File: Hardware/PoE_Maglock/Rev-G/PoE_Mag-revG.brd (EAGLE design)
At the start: 72.8 x 47.9 mm, 85 parts, among them IC2 ATMEGA32U4-MU, J2 1X2-3.5MM, J3 1X2-3.5MM, J4 1X2-3.5MM, J5 1X2-3.5MM, J6 10103594-0001LF, Q1 35A/25V/8.5mΩ, Q3 35A/25V/8.5mΩ, Q5 35A/25V/8.5mΩ, Q6 35A/25V/8.5mΩ, SW1 SPST_TACT-KMR2, U4 W5500, X2 J1011FHY931147C, Y4 8MHz

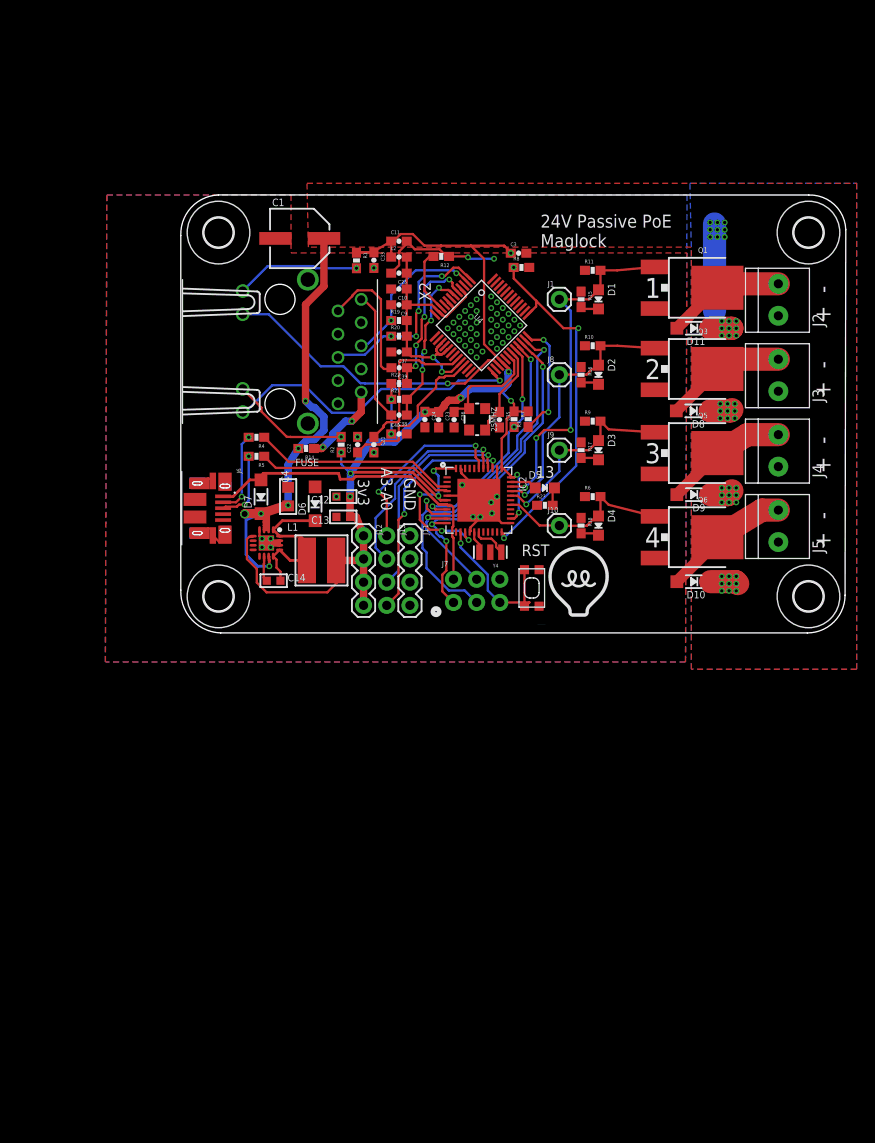
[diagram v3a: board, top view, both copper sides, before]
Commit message: HEEP-1046 added analog terminal blocks to schematic
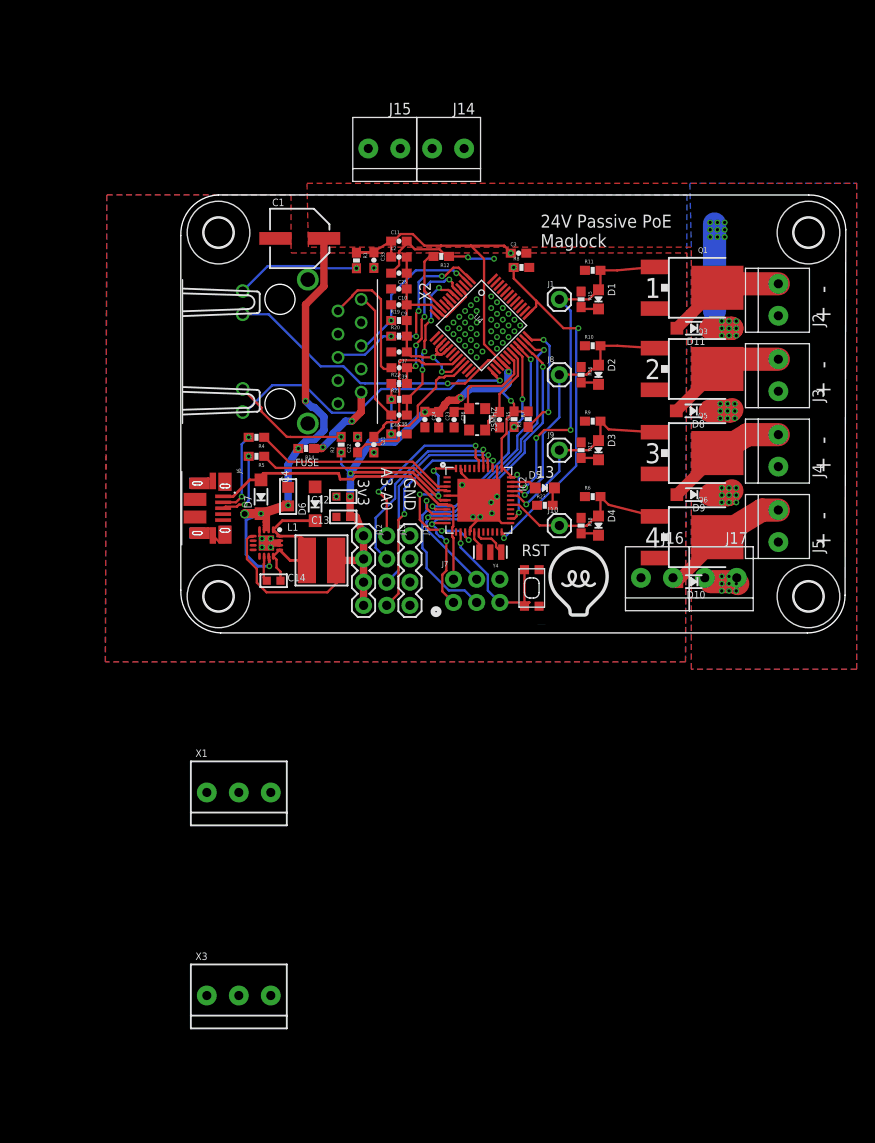
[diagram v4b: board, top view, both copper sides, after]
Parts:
- added J14, J15, J16, J17: 1X2-3.5MM, adafruit:1X2-3.5MM
- added X1, X3: (no value), microbuilder:TERMBLOCK_1X3-3.5MM
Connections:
- removed net 0: IC2.20
- removed net 1: IC2.21
- removed net 2: IC2.19
- removed net 3: IC2.18
- new net 0/RX: IC2.20, J17.2
- new net 1/TX: IC2.21, J17.1
- new net 2/SDA: IC2.19, J15.1
- new net 3/SCL: IC2.18, J15.2
- net +3V3: now also J14.1, J16.1, X1.3, X3.3
- net GND: now also J14.2, J16.2, X1.1, X3.1

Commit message: HEEP-1046 added DC jack to schematic and to brd. not yet positioned
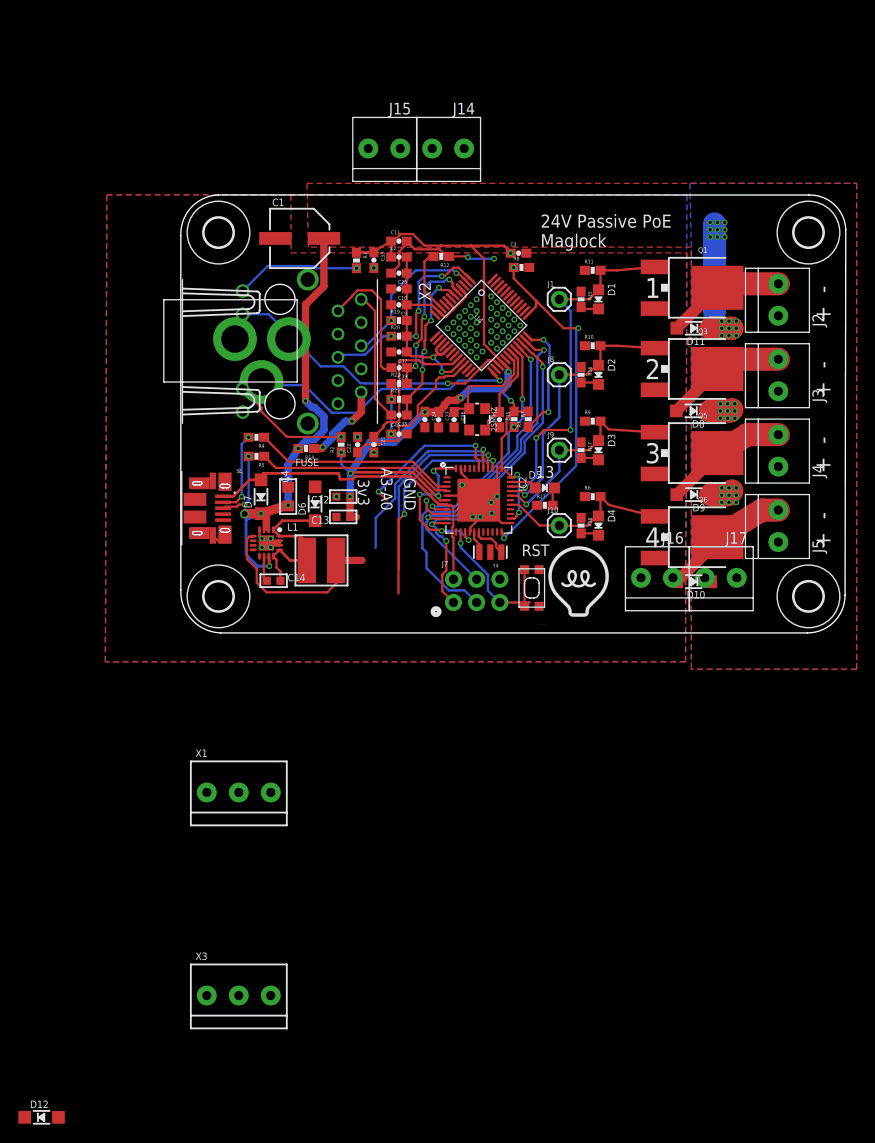
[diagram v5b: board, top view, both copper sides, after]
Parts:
- removed J11, J12: (no value), SparkFun-Connectors:1X04
- removed J13: (no value), SparkFun-Connectors:1X04_NO_SILK
- added D12: PMEG4030ER, microbuilder:SOD-123
- added U$4: 2.1MMJACKTHM, adafruit:PJ-102A
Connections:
- new net N$1: D12.A, U$4.TIP
- net +3V3: no longer J12.1, J12.2, J12.3, J12.4
- net A0: no longer J13.4
- net A1: no longer J13.3
- net A2: no longer J13.2
- net A3: no longer J13.1
- net GND: now also U$4.RING, U$4.RING_SW; no longer J11.1, J11.2, J11.3, J11.4
- net VBAT: now also D12.C
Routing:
- net +3V3: track 148.3 -> 137.4 mm
- net A3: track 20.5 -> 16.6 mm
- net VBAT: track 77.9 -> 74.8 mm, vias 51 -> 42
- net A1: track 24.3 -> 22.4 mm
- net A0: track 25.4 -> 23.6 mm
- net A2: track 22.9 -> 21.2 mm

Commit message: HEEP-1046 extended southside
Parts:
- added J11: 1X2-3.5MM, adafruit:1X2-3.5MM
- moved D12 66.1 mm to (2.54, 10.8), turned to 90 degrees
- moved U$15 57.9 mm to (46.7, 57.8)
- moved X3 49.8 mm to (33.4, 3.81)
- moved X1 24.7 mm to (21.6, 3.81)
- moved J6 8.25 mm to (6.25, 21.0)
- moved C1 7.94 mm to (17.5, 50.2)
- moved C3 7.62 mm to (41.4, 48.2)
- moved C33 7.62 mm to (25.6, 47.5)
- moved D11 7.62 mm to (60.6, 40.0)
- moved H1 7.62 mm to (73.1, 50.5)
- moved H3 7.62 mm to (8.57, 50.5)
- moved Q1 7.62 mm to (61.6, 44.5)
- moved X2 7.62 mm to (15.3, 37.5)
- moved 25MHZ 7.62 mm to (36.9, 30.0)
- moved C21 7.62 mm to (25.6, 27.3)
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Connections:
- removed net N$2: R14.1, X2.9
- new net POE+: D12.C, R14.1, X2.9
- net GND: now also J11.2
- net VBAT: now also J11.1; no longer D12.C
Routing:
- net VBAT: track 74.8 -> 56.5 mm, vias 42 -> 41
- net POE+: track 0.00 -> 9.23 mm, vias 0 -> 2
- net N$2: track 9.23 -> 0.00 mm, vias 2 -> 0
- net A1: track 22.4 -> 13.3 mm
- net A0: track 23.6 -> 14.6 mm, vias 2 -> 1
- net A2: track 21.2 -> 13.4 mm
- net +3V3: track 137.4 -> 139.3 mm
- net A3: track 16.6 -> 15.3 mm, vias 2 -> 1
- net N$13: track 9.10 -> 8.47 mm
- net VBUS: track 37.2 -> 36.6 mm
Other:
- board size 72.8 x 47.9 mm -> 72.8 x 53.3 mm

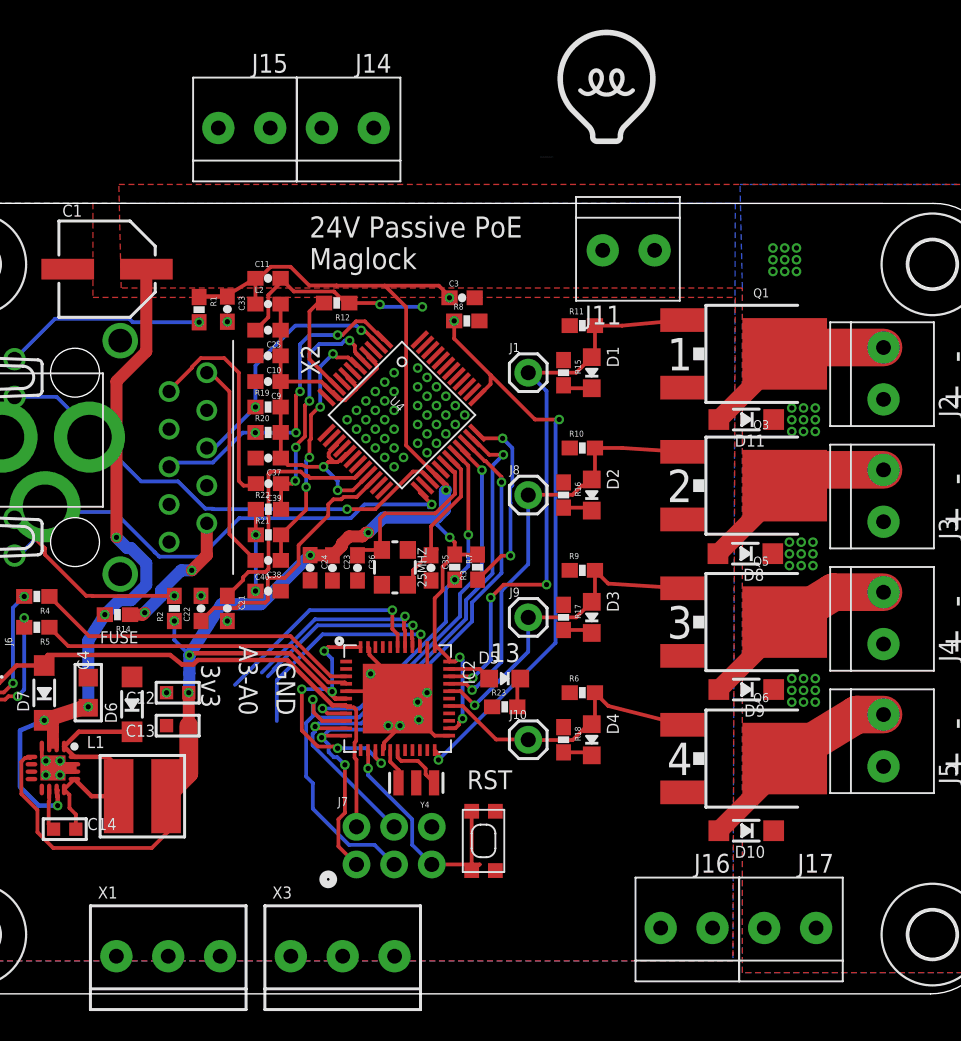
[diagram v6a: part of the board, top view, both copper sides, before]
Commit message: HEEP-1046 before rotating buck circuit 90 degrees
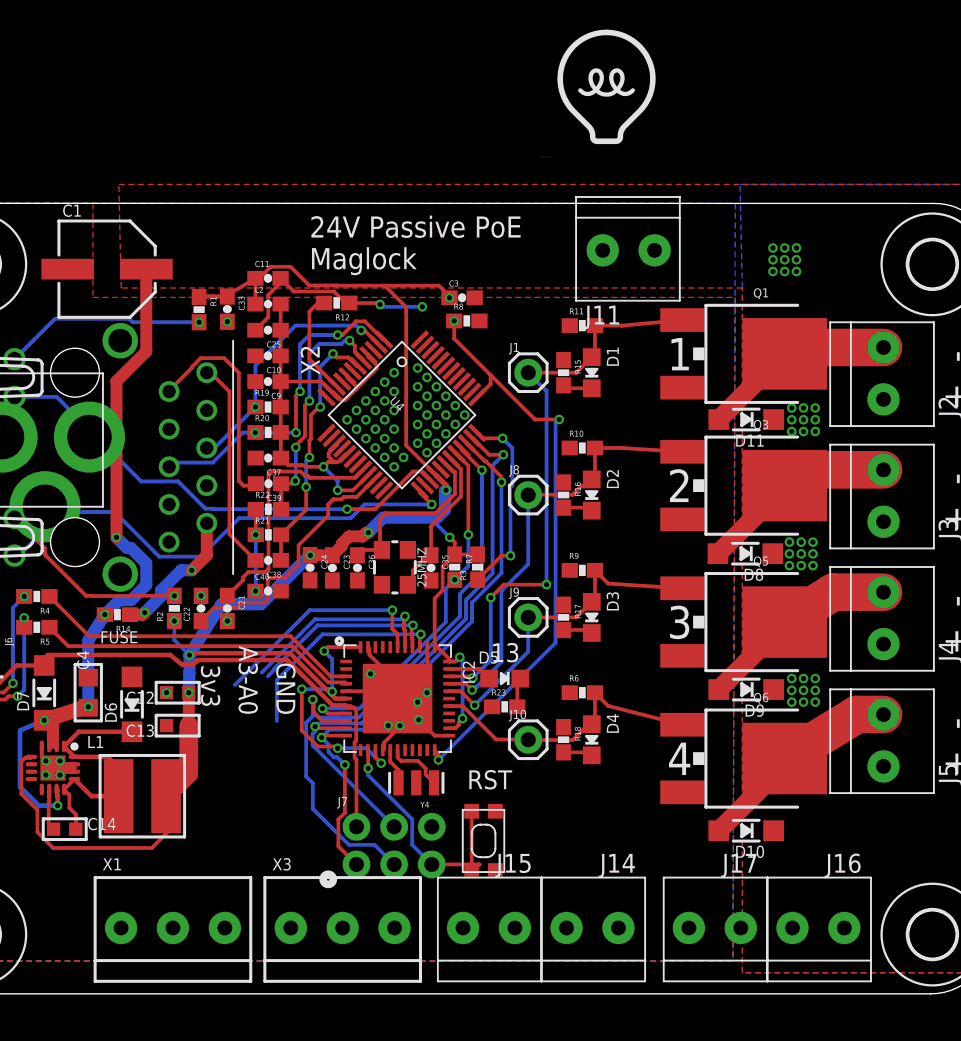
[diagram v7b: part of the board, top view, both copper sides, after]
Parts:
- moved J14 56.4 mm to (50.2, 5.71)
- moved J15 56.4 mm to (43.2, 5.71)
- moved J16 8.89 mm to (65.4, 5.71)
- moved J17 5.08 mm to (58.4, 5.71)
- moved X1 1.93 mm to (21.9, 5.71)
- moved X3 1.90 mm to (33.4, 5.71)
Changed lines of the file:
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@@
 <attribute name="VALUE" x="19.178175" y="27.998" size="0.8128" layer="27" font="vector" rot="R180"/>
 </element>
-<element name="J14" library="adafruit" library_urn="urn:adsk.eagle:library:420" package="1X2-3.5MM" value="1X2-3.5MM" x="33.655" y="59.69"/>
-<element name="J15" library="adafruit" library_urn="urn:adsk.eagle:library:420" package="1X2-3.5MM" value="1X2-3.5MM" x="26.67" y="59.69"/>
-<element name="J16" library="adafruit" library_urn="urn:adsk.eagle:library:420" package="1X2-3.5MM" value="1X2-3.5MM" x="56.515" y="5.715"/>
-<element name="J17" library="adafruit" library_urn="urn:adsk.eagle:library:420" package="1X2-3.5MM" value="1X2-3.5MM" x="63.5" y="5.715"/>
-<element name="X1" library="microbuilder" package="TERMBLOCK_1X3-3.5MM" value="" x="21.59" y="3.81"/>
-<element name="X3" library="microbuilder" package="TERMBLOCK_1X3-3.5MM" value="" x="33.36" y="3.81"/>
+<element name="J14" library="adafruit" library_urn="urn:adsk.eagle:library:420" package="1X2-3.5MM" value="1X2-3.5MM" x="50.165" y="5.715"/>
+<element name="J15" library="adafruit" library_urn="urn:adsk.eagle:library:420" package="1X2-3.5MM" value="1X2-3.5MM" x="43.18" y="5.715"/>
+<element name="J16" library="adafruit" library_urn="urn:adsk.eagle:library:420" package="1X2-3.5MM" value="1X2-3.5MM" x="65.405" y="5.715"/>
+<element name="J17" library="adafruit" library_urn="urn:adsk.eagle:library:420" package="1X2-3.5MM" value="1X2-3.5MM" x="58.42" y="5.715"/>
+<element name="X1" library="microbuilder" package="TERMBLOCK_1X3-3.5MM" value="" x="21.9075" y="5.715"/>
+<element name="X3" library="microbuilder" package="TERMBLOCK_1X3-3.5MM" value="" x="33.36" y="5.715"/>
 <element name="U$4" library="adafruit" library_urn="urn:adsk.eagle:library:420" package="PJ-102A" value="2.1MMJACKTHM" x="6.985" y="38.735" rot="R90"/>
 <element name="D12" library="microbuilder" package="SOD-123" value="PMEG4030ER" x="2.54" y="10.795" rot="R90"/>
@@
 <contactref element="U$4" pad="RING_SW"/>
 <contactref element="J11" pad="2"/>
-<wire x1="29.172175" y1="49.547496875" x2="31.955" y2="59.69" width="0" layer="19" extent="1-1"/>
-<wire x1="54.815" y1="5.715" x2="56.285" y2="14.865" width="0" layer="19" extent="1-1"/>
+<wire x1="56.285" y1="14.865" x2="63.705" y2="5.715" width="0" layer="19" extent="1-1"/>
 </signal>
 <signal name="RD-">
@@
 <contactref element="IC2" pad="19"/>
 <contactref element="J15" pad="1"/>
-<wire x1="38.0665125" y1="17.71625" x2="28.47" y2="59.69" width="0" layer="19" extent="1-1"/>
+<wire x1="44.98" y1="5.715" x2="38.0665125" y2="17.71625" width="0" layer="19" extent="1-1"/>
 </signal>
 <signal name="N$6">
@@
 <contactref element="IC2" pad="21"/>
 <contactref element="J17" pad="1"/>
-<wire x1="39.0665125" y1="17.71625" x2="65.3" y2="5.715" width="0" layer="19" extent="1-1"/>
+<wire x1="39.0665125" y1="17.71625" x2="60.22" y2="5.715" width="0" layer="19" extent="1-1"/>
 </signal>
 <signal name="0/RX">
 <contactref element="IC2" pad="20"/>
 <contactref element="J17" pad="2"/>
-<wire x1="38.5665125" y1="17.71625" x2="61.8" y2="5.715" width="0" layer="19" extent="1-1"/>
+<wire x1="38.5665125" y1="17.71625" x2="56.72" y2="5.715" width="0" layer="19" extent="1-1"/>
 </signal>
 <signal name="+3V3">
@@
 <wire x1="21.44375" y1="14.605" x2="22.975" y2="16.13625" width="1.27" layer="1"/>
 <wire x1="22.975" y1="16.13625" x2="22.975" y2="19.3675" width="1.27" layer="1"/>
-<wire x1="36.195" y1="49.05375" x2="35.455" y2="59.69" width="0" layer="19" extent="1-1"/>
-<wire x1="18.09" y1="3.81" x2="20.47875" y2="11.1125" width="0" layer="19" extent="1-1"/>
-<wire x1="29.86" y1="3.81" x2="18.09" y2="3.81" width="0" layer="19" extent="1-1"/>
-<wire x1="58.315" y1="5.715" x2="41.2209125" y2="19.45051875" width="0" layer="19" extent="1-1"/>
+<wire x1="51.965" y1="5.715" x2="67.205" y2="5.715" width="0" layer="19" extent="1-1"/>
+<wire x1="40.96164375" y1="19.19125" x2="51.965" y2="5.715" width="0" layer="19" extent="1-1"/>
+<wire x1="18.4075" y1="5.715" x2="20.47875" y2="11.1125" width="0" layer="19" extent="1-1"/>
+<wire x1="29.86" y1="5.715" x2="21.59" y2="12.22375" width="0" layer="19" extent="1-1"/>
 </signal>
 <signal name="13">
@@
 <contactref element="IC2" pad="18"/>
 <contactref element="J15" pad="2"/>
-<wire x1="37.5665125" y1="17.71625" x2="24.97" y2="59.69" width="0" layer="19" extent="1-1"/>
+<wire x1="41.48" y1="5.715" x2="37.5665125" y2="17.71625" width="0" layer="19" extent="1-1"/>
 </signal>
 <signal name="D4">

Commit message: HEEP-1046 stopping for the night to focus on JW
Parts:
- removed U$4: 2.1MMJACKTHM, adafruit:PJ-102A
- added X4: (no value), microbuilder:DCJACK_2MM_PTH
- moved R4 19.0 mm to (14.7, 9.19), turned to 90 degrees
- moved R5 16.8 mm to (13.0, 9.19), turned to 90 degrees
- moved C14 13.1 mm to (27.6, 13.3), turned to 90 degrees
- moved D7 10.9 mm to (18.4, 12.0), turned to 180 degrees
- moved U$19 10.5 mm to (23.5, 12.5), turned to 0 degrees
- moved J6 9.21 mm to (6.25, 11.7)
- moved C4 7.03 mm to (18.4, 14.9), turned to 180 degrees
- moved L1 6.83 mm to (25.4, 18.6), turned to 90 degrees
- moved SW1 4.29 mm to (47.1, 11.4), turned to 0 degrees
- moved C12 3.86 mm to (18.4, 21.0), turned to 270 degrees
- moved D6 2.93 mm to (19.2, 17.9), turned to 180 degrees
- moved C13 2.25 mm to (20.6, 21.0), turned to 270 degrees
- moved H2 1.27 mm to (8.57, 4.00)
- moved H4 1.27 mm to (73.1, 4.00)
- moved X1 0.16 mm to (21.7, 5.71)
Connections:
- net GND: now also X4.GND, X4.GNDBREAK; no longer U$4.RING, U$4.RING_SW
- net N$1: now also X4.PWR; no longer U$4.TIP
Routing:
- net VBUS: track 36.6 -> 16.8 mm
- net D-: track 22.3 -> 4.87 mm
- net D+: track 21.6 -> 4.71 mm
- net A0: track 14.6 -> 7.51 mm
- net A3: track 15.3 -> 8.22 mm
- net N$13: track 8.47 -> 2.29 mm, vias 2 -> 1
- net RST: track 17.4 -> 23.5 mm
- net A1: track 13.3 -> 7.95 mm
- net A2: track 13.4 -> 8.29 mm
- net N$6: track 7.97 -> 3.12 mm, vias 2 -> 1
- net VBAT: track 56.5 -> 52.0 mm
- net +3V3: track 139.3 -> 136.7 mm
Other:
- board size 72.8 x 53.3 mm -> 72.8 x 54.6 mm
- board text added: "RESET"
- board text removed: "3v3"
- board text removed: "A3-A0"
- board text removed: "RST"
